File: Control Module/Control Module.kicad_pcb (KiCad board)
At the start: 2 copper layers, 99.6 x 99.6 mm, 69 parts, among them J1 USB_B, J2 Conn_01x22, J3 Conn_01x22, SW1 SW_Push, U1 74LS161, U10 74LS30, U11 74LS08, U12 74LS08, U13 74LS08, U2 74LS173, U3 74LS273, U4 28C256, U5 28C256, U6 74LS08, U7 74LS04, U8 74LS02, U9 74LS02

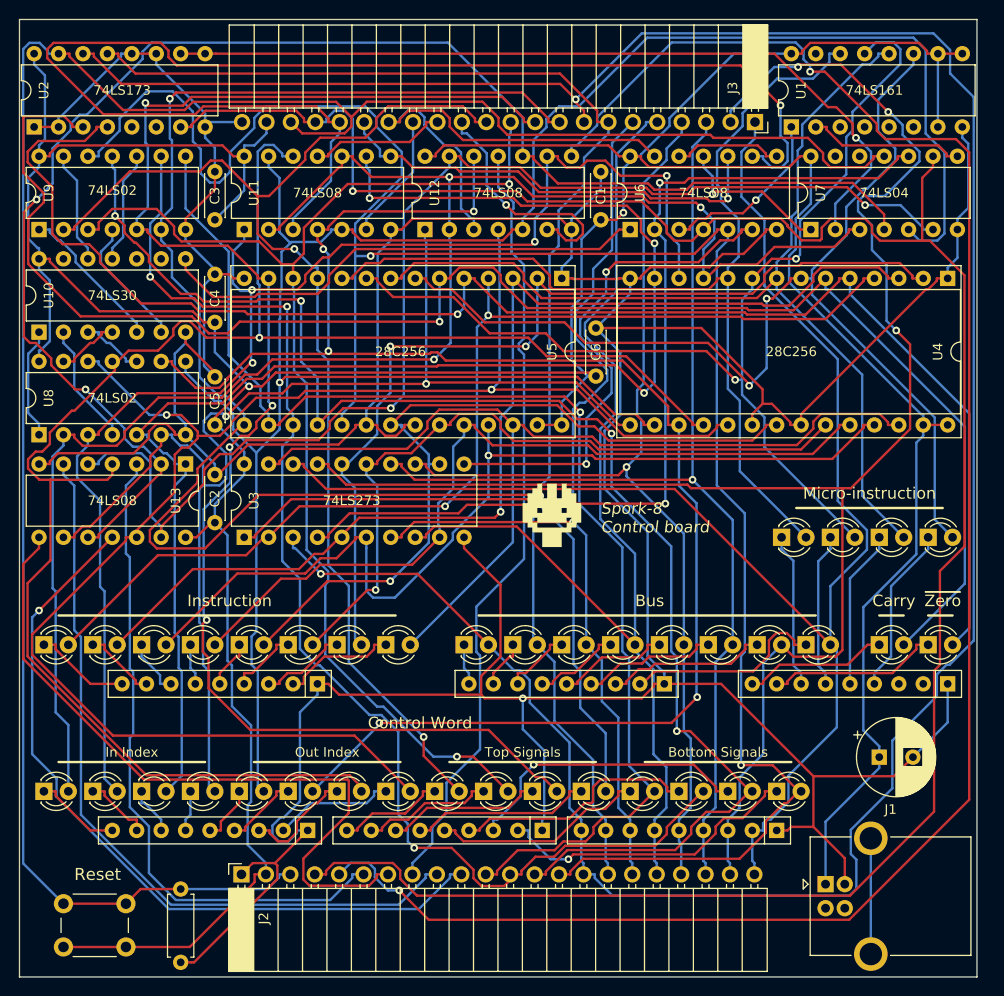
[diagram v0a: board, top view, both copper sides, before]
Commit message: Fixed floating inputs; improved power; added parts list; replaced JK latches
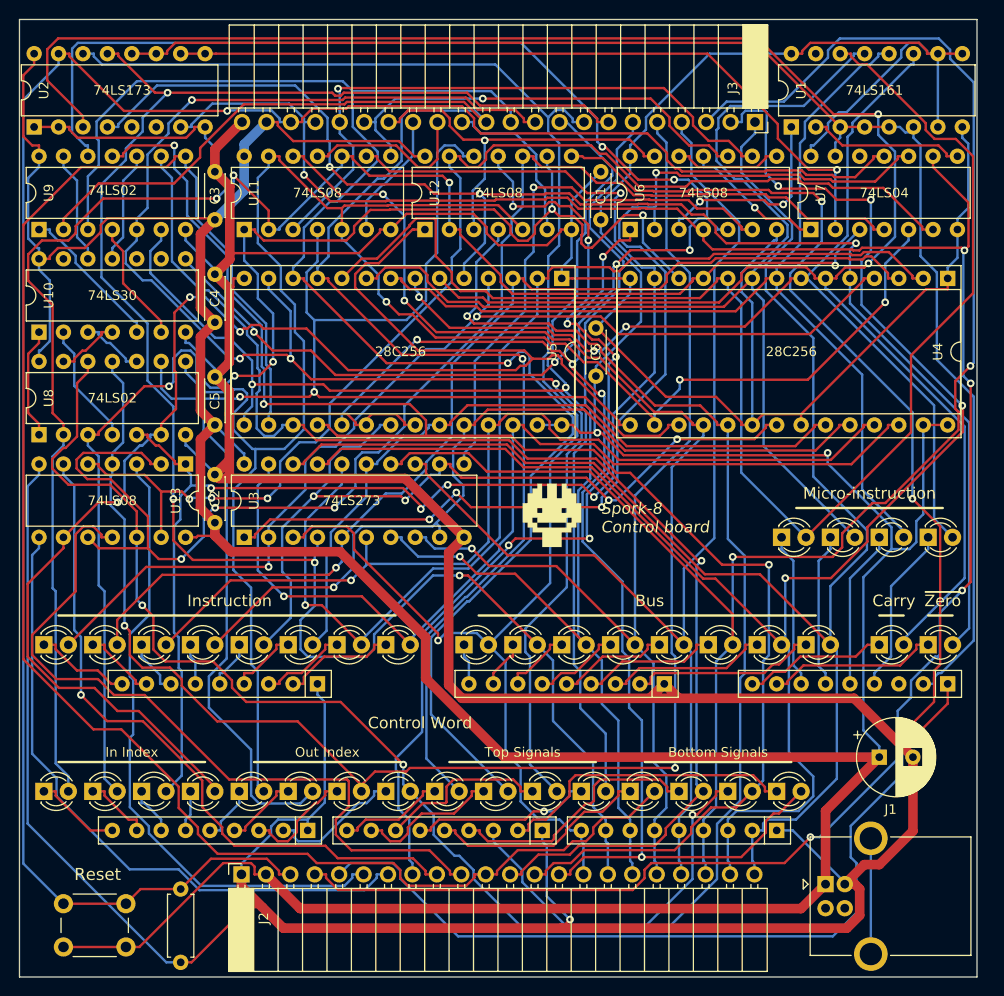
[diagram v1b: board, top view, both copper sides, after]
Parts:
- C8: value 1mF -> 1000uF
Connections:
- RN1 pad 2: Net-(RN1-Pad2) -> GND_1k
- U1 pad 3: Net-(U1-Pad3) -> GND_1k
- U1 pad 4: Net-(U1-Pad4) -> GND_1k
- U1 pad 5: Net-(U1-Pad5) -> GND_1k
- U1 pad 6: Net-(U1-Pad6) -> GND_1k
- U2 pad 11: GND -> GND_1k
- U2 pad 12: GND -> GND_1k
- U7 pad 12: (no net) -> Net-(U7-Pad12)
- U7 pad 13: (no net) -> GND_1k
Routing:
- net GND_1k: track 0.00 -> 152.5 mm
- net BUS0: track 276.3 -> 175.3 mm, vias 2 -> 1
- net GND: track 497.7 -> 581.3 mm
- net TOP_SIG_IN_0: track 138.5 -> 64.6 mm
- net BUS5: track 114.1 -> 181.8 mm, vias 1 -> 2
- net VCC: track 440.5 -> 504.1 mm
- net CW12: track 130.4 -> 179.3 mm, vias 1 -> 0
- net Net-(D5-Pad2): track 165.6 -> 212.9 mm, vias 1 -> 2
- net CW9: track 126.6 -> 169.4 mm, vias 2 -> 1
- net Net-(D1-Pad2): track 106.9 -> 146.0 mm
- net CW7: track 168.4 -> 206.7 mm, vias 2 -> 3
- net CW11: track 173.9 -> 138.0 mm
- net CW8: track 126.5 -> 157.6 mm, vias 2 -> 1
- net BUS1: track 164.7 -> 195.4 mm, vias 1 -> 4
- net CW3: track 130.7 -> 157.8 mm, vias 2 -> 3
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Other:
- rule pad_to_mask_clearance: 0.051 -> 0

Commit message: Revise control and RAM modules
- Change control signals on low going clock
- Pull down control signals with 1k resistors
- AND the write signal with clock on RAM / ROM module
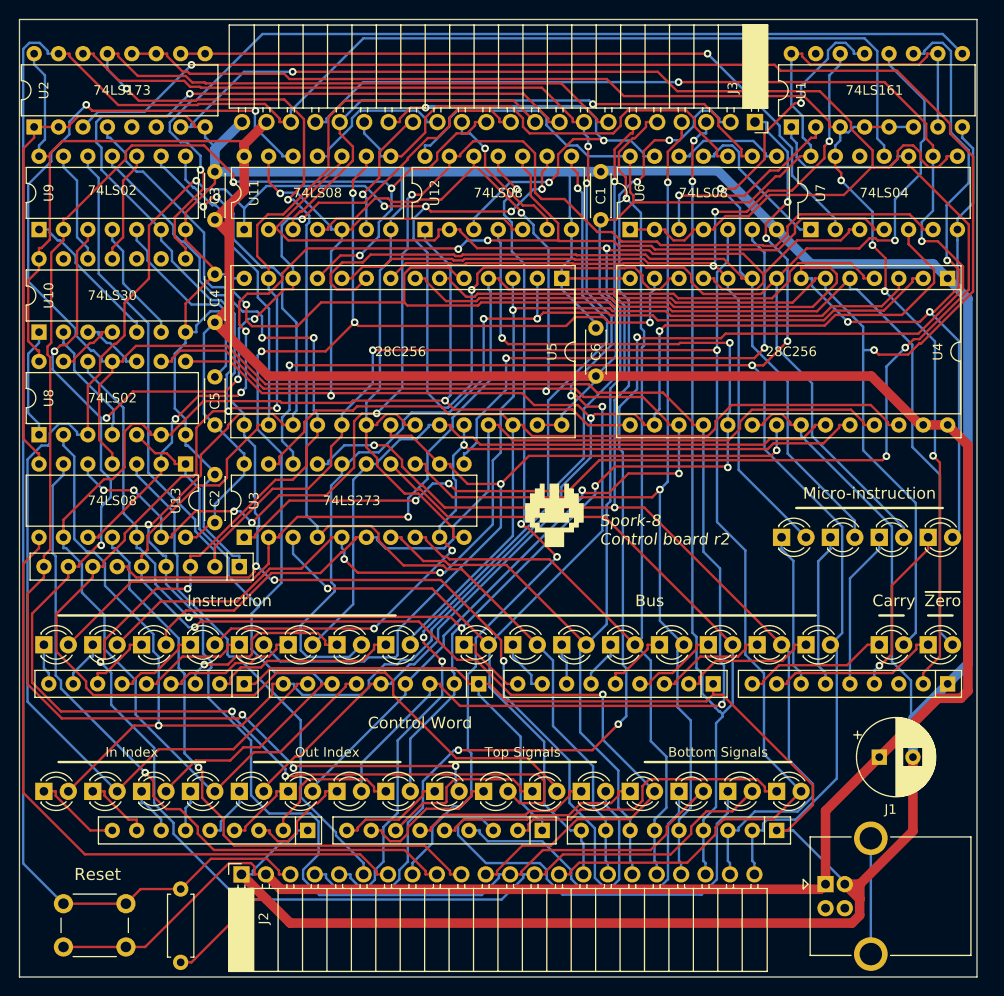
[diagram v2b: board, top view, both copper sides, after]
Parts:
- added RN7: 1k, Resistor_THT:R_Array_SIP9, F.Cu at (73.7, 100.1)
- added RN8: 1k, Resistor_THT:R_Array_SIP9, F.Cu at (48.8, 87.9)
- R1, RN2: value 100k -> 1k
- moved RN3 7.62 mm to (49.3, 100.1)
- moved RN6 5.08 mm to (98.0, 100.1)
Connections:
- U1 pad 1: ~MI_RESET -> ~RESET
- U1 pad 2: ~CLOCK -> MI_CLOCK
- U1 pad 9: VCC -> ~CWZ
- U2 pad 7: CLOCK -> ~CLOCK
- U6 pad 1: ~CWZ -> ~CLOCK
- U6 pad 2: ~RESET -> ~CLOCK
- U6 pad 3: ~MI_RESET -> MI_CLOCK
- U6 pad 4: CLOCK -> ~CLOCK
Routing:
- net ~CLOCK: track 16.3 -> 121.5 mm, vias 0 -> 1
- net BOTTOM_SIG_IN_0: track 172.9 -> 93.1 mm
- net CW1: track 147.2 -> 211.2 mm, vias 5 -> 6
- net CW11: track 138.0 -> 191.1 mm, vias 2 -> 4
- net BUS5: track 181.8 -> 132.4 mm
- net VCC: track 504.1 -> 455.6 mm, vias 2 -> 0
- net CW0: track 170.2 -> 216.1 mm, vias 4 -> 2
- net CW7: track 206.7 -> 163.3 mm, vias 3 -> 6
- net ~CWZ: track 61.9 -> 104.8 mm, vias 3 -> 1
- net Net-(D1-Pad2): track 146.0 -> 103.3 mm, vias 0 -> 3
- net CW12: track 179.3 -> 142.7 mm, vias 0 -> 2
- net BUS6: track 175.3 -> 141.9 mm
- net GND: track 581.3 -> 611.2 mm, vias 1 -> 0
- net CW15: track 231.8 -> 207.3 mm, vias 8 -> 2
- net ~CW0: track 140.2 -> 118.1 mm, vias 3 -> 5
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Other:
- board text added: "Spork-8 Control board r2"
- board text removed: "Spork-8 Control board"

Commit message: Update all boards to r3, and update revision log and gitignore
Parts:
- removed RN7, RN8: 1k, Resistor_THT:R_Array_SIP9
- removed U10: 74LS30, Package_DIP:DIP-14_W7.62mm
- added HOLE1: MountingHole_2.2mm_M2_DIN965_Pad, MountingHole:MountingHole_2.2mm_M2_DIN965_Pad, F.Cu at (75.4, 49.3)
- added HOLE2: MountingHole_2.2mm_M2_DIN965_Pad, MountingHole:MountingHole_2.2mm_M2_DIN965_Pad, F.Cu at (30.7, 102.9)
- added HOLE3: MountingHole_2.2mm_M2_DIN965_Pad, MountingHole:MountingHole_2.2mm_M2_DIN965_Pad, F.Cu at (118.6, 108.0)
- added R2: 5.1k, Resistor_SMD:R_0603_1608Metric, F.Cu at (118.0, 115.6)
- added R3: 5.1k, Resistor_SMD:R_0603_1608Metric, F.Cu at (118.0, 128.0)
- J1: value USB_B -> USB_C_PowerOnly_6P; footprint Connector_USB:USB_B_OST_USB-B1HSxx_Horizontal -> updated_libs:USB_C_Receptacle_G-Switch_GT-USB-7010ASV
- U1: value 74LS161 -> 74HC161
- U11, U12, U13, U6: value 74LS08 -> 74HC08
- U2: value 74LS173 -> 74HC173
- U3: value 74LS273 -> 74HC173; footprint Package_DIP:DIP-20_W7.62mm -> Package_DIP:DIP-16_W7.62mm
- U7: value 74LS04 -> 74HC04
- U8: value 74LS02 -> 74HC173; footprint Package_DIP:DIP-14_W7.62mm -> Package_DIP:DIP-16_W7.62mm
- moved U6 62.4 mm to (27.9, 63.5)
- moved D20 44.7 mm to (98.6, 111.3)
- moved D21 44.7 mm to (103.6, 111.3)
- moved D22 44.7 mm to (108.7, 111.3)
- moved D19 44.7 mm to (93.5, 111.3)
- moved D17 43.7 mm to (82.3, 111.3)
- moved D18 43.7 mm to (87.4, 111.3)
- moved D15 43.7 mm to (72.1, 111.3)
- moved D16 43.7 mm to (77.2, 111.3)
- moved D24 40.6 mm to (33.5, 111.3)
- moved D25 40.6 mm to (38.6, 111.3)
- moved D26 40.6 mm to (43.7, 111.3)
- moved D23 40.6 mm to (28.4, 111.3)
- moved D27 39.6 mm to (49.8, 111.3)
- moved D28 39.6 mm to (54.9, 111.3)
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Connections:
- net ~CW0 renamed ~{CW0}
- net ~CW4 renamed ~{CW4}
- net ~FR_IN renamed ~{FR_IN}
- D1 pad 2: Net-(D1-Pad2) -> Net-(D1-A)
- D10 pad 2: Net-(D10-Pad2) -> INST4
- D11 pad 2: Net-(D11-Pad2) -> INST3
- D12 pad 2: Net-(D12-Pad2) -> INST2
- D13 pad 2: Net-(D13-Pad2) -> INST1
- D14 pad 2: Net-(D14-Pad2) -> INST0
- D15 pad 2: CW0 -> CW7
- D16 pad 2: CW1 -> CW6
- D17 pad 2: CW2 -> CW5
- D18 pad 2: CW3 -> CW4
- D19 pad 2: CW4 -> CW3
- D2 pad 2: Net-(D2-Pad2) -> Net-(D2-A)
- D20 pad 2: CW5 -> CW2
- D21 pad 2: CW6 -> CW1
- D22 pad 2: CW7 -> CW0
- D23 pad 2: CW8 -> CW15
- D24 pad 2: CW9 -> CW14
- D25 pad 2: CW10 -> CW13
- D26 pad 2: CW11 -> CW12
- D27 pad 2: CW12 -> CW11
- D28 pad 2: CW13 -> CW10
- D29 pad 2: CW14 -> CW9
- D3 pad 2: Net-(D3-Pad2) -> Net-(D3-A)
- D30 pad 2: CW15 -> CW8
- D31 pad 2: BUS0 -> BUS7
- D32 pad 2: BUS1 -> BUS6
- D33 pad 2: BUS2 -> BUS5
- D34 pad 2: BUS3 -> BUS4
- D35 pad 2: BUS4 -> BUS3
- D36 pad 2: BUS5 -> BUS2
- D37 pad 2: BUS6 -> BUS1
- D38 pad 2: BUS7 -> BUS0
- D4 pad 2: Net-(D4-Pad2) -> Net-(D4-A)
- D5 pad 2: Net-(D5-Pad2) -> Net-(D5-A)
- D6 pad 2: Net-(D6-Pad2) -> Net-(D6-A)
- D7 pad 2: Net-(D7-Pad2) -> INST7
- D8 pad 2: Net-(D8-Pad2) -> INST6
- D9 pad 2: Net-(D9-Pad2) -> INST5
- RN1 pad 3: Net-(RN1-Pad3) -> unconnected-(RN1-R2-Pad3)
- U1 pad 1: ~RESET -> ~{RESET}
- U1 pad 11: Net-(D4-Pad2) -> Net-(D1-A)
- U1 pad 12: Net-(D3-Pad2) -> Net-(D2-A)
- U1 pad 13: Net-(D2-Pad2) -> Net-(D3-A)
- U1 pad 14: Net-(D1-Pad2) -> Net-(D4-A)
- U1 pad 15: Net-(U1-Pad15) -> unconnected-(U1-TC-Pad15)
- U1 pad 9: ~CWZ -> ~{CW14}
- U2 pad 3: Net-(D5-Pad2) -> Net-(D6-A)
- U2 pad 4: Net-(D6-Pad2) -> Net-(D5-A)
- U2 pad 5: Net-(U2-Pad5) -> unconnected-(U2-Q2-Pad5)
- U2 pad 6: Net-(U2-Pad6) -> unconnected-(U2-Q3-Pad6)
- U2 pad 7: ~CLOCK -> ~{CLOCK}
- U3 pad 1: ~RESET -> GND
- U3 pad 10: GND -> CW15
- U3 pad 11: IR_IN -> BUS3
- U3 pad 12: Net-(D11-Pad2) -> BUS2
- U3 pad 13: BUS4 -> BUS1
- U3 pad 14: BUS5 -> BUS0
- U3 pad 15: Net-(D12-Pad2) -> RESET
- U3 pad 16: Net-(D13-Pad2) -> VCC
- U3 pad 2: Net-(D7-Pad2) -> GND
- U3 pad 3: BUS0 -> INST0
- U3 pad 4: BUS1 -> INST1
- U3 pad 5: Net-(D8-Pad2) -> INST2
- U3 pad 6: Net-(D9-Pad2) -> INST3
- U3 pad 7: BUS2 -> ~{CLOCK}
- U3 pad 8: BUS3 -> GND
- U3 pad 9: Net-(D10-Pad2) -> CW15
- U4 pad 10: Net-(D1-Pad2) -> Net-(D4-A)
- U4 pad 2: Net-(D13-Pad2) -> INST6
- U4 pad 21: Net-(D11-Pad2) -> INST4
- U4 pad 23: Net-(D12-Pad2) -> INST5
- U4 pad 24: Net-(D10-Pad2) -> INST3
- U4 pad 25: Net-(D9-Pad2) -> INST2
- U4 pad 26: Net-(D14-Pad2) -> INST7
- U4 pad 3: Net-(D8-Pad2) -> INST1
- U4 pad 4: Net-(D7-Pad2) -> INST0
- U4 pad 5: Net-(D6-Pad2) -> Net-(D5-A)
- U4 pad 6: Net-(D5-Pad2) -> Net-(D6-A)
- U4 pad 7: Net-(D4-Pad2) -> Net-(D1-A)
- U4 pad 8: Net-(D3-Pad2) -> Net-(D2-A)
- U4 pad 9: Net-(D2-Pad2) -> Net-(D3-A)
- U5 pad 10: Net-(D1-Pad2) -> Net-(D4-A)
- U5 pad 2: Net-(D13-Pad2) -> INST6
- U5 pad 21: Net-(D11-Pad2) -> INST4
- U5 pad 23: Net-(D12-Pad2) -> INST5
- U5 pad 24: Net-(D10-Pad2) -> INST3
- U5 pad 25: Net-(D9-Pad2) -> INST2
- U5 pad 26: Net-(D14-Pad2) -> INST7
- U5 pad 3: Net-(D8-Pad2) -> INST1
- U5 pad 4: Net-(D7-Pad2) -> INST0
- U5 pad 5: Net-(D6-Pad2) -> Net-(D5-A)
- U5 pad 6: Net-(D5-Pad2) -> Net-(D6-A)
- U5 pad 7: Net-(D4-Pad2) -> Net-(D1-A)
- U5 pad 8: Net-(D3-Pad2) -> Net-(D2-A)
- U5 pad 9: Net-(D2-Pad2) -> Net-(D3-A)
- U6 pad 1: ~CLOCK -> ~{CLOCK}
- U6 pad 2: ~CLOCK -> ~{CLOCK}
- U6 pad 4: ~CLOCK -> GND
- U6 pad 5: CW15 -> GND
- U6 pad 6: IR_IN -> unconnected-(U6-Pad6)
- U7 pad 10: ~RESET -> ~{RESET}
- U7 pad 12: Net-(U7-Pad12) -> ~{CW14}
- U7 pad 13: GND_1k -> CW14
- U7 pad 8: ~CLOCK -> ~{CLOCK}
- U8 pad 1: Net-(U10-Pad1) -> GND
- U8 pad 10: Net-(U10-Pad3) -> CW15
- U8 pad 11: CW6 -> BUS7
- U8 pad 12: CW7 -> BUS6
- U8 pad 13: Net-(U10-Pad4) -> BUS5
- U8 pad 14: VCC -> BUS4
- U8 pad 2: CW0 -> GND
- U8 pad 3: CW1 -> INST4
- U8 pad 4: Net-(U10-Pad2) -> INST5
- U8 pad 5: CW2 -> INST6
- U8 pad 6: CW3 -> INST7
- U8 pad 7: GND -> ~{CLOCK}
- U8 pad 8: CW4 -> GND
- U8 pad 9: CW5 -> CW15
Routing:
- net Net-(D5-Pad2): track 213.4 -> 0.00 mm, vias 2 -> 0
- net ~{CLOCK}: track 0.00 -> 211.7 mm, vias 0 -> 3
- net INST6: track 0.00 -> 163.2 mm, vias 0 -> 10
- net Net-(D6-Pad2): track 146.7 -> 0.00 mm, vias 1 -> 0
- net Net-(D6-A): track 0.00 -> 139.9 mm, vias 0 -> 1
- net Net-(D5-A): track 0.00 -> 135.0 mm, vias 0 -> 3
- net Net-(D2-A): track 0.00 -> 130.9 mm, vias 0 -> 2
- net Net-(D4-Pad2): track 129.6 -> 0.00 mm, vias 3 -> 0
- net ~RESET: track 125.0 -> 0.00 mm, vias 4 -> 0
- net ~CLOCK: track 121.5 -> 0.00 mm, vias 1 -> 0
- net Net-(D1-A): track 0.00 -> 120.9 mm, vias 0 -> 2
- net Net-(D2-Pad2): track 119.0 -> 0.00 mm, vias 2 -> 0
- net Net-(D8-Pad2): track 117.9 -> 0.00 mm, vias 3 -> 0
- net Net-(D3-A): track 0.00 -> 116.0 mm, vias 0 -> 2
- net Net-(D7-Pad2): track 115.0 -> 0.00 mm, vias 1 -> 0
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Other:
- net class Default removed
- board text added: "Spork-8 Control board r3"
- board text added: "Zero"
- board text removed: "Spork-8 Control board r2"
- board text removed: "~Zero"
